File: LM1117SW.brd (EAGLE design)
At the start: 160 x 100 mm, 7 parts

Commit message: layout stuff
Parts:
- R1, R2: device rcl:R0402 -> rcl:R0603
- moved C1 33.5 mm to (2.32, 5.55), turned to 90 degrees
- moved C2 29.7 mm to (4.20, 5.55), turned to 90 degrees
- moved R2 28.9 mm to (1.89, 2.18), flipped to the bottom, turned to 90 degrees
- moved L1 27.9 mm to (3.55, 5.56), flipped to the bottom, turned to 90 degrees
- moved R1 27.7 mm to (4.50, 2.19), flipped to the bottom, turned to 270 degrees
- moved U$2 26.9 mm to (3.16, 2.04), turned to 270 degrees
- moved U$1 16.9 mm to (9.58, 3.98), turned to 270 degrees
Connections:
- net N$2 renamed VOUT
- net N$3 renamed SENS
- net N$4 renamed VIN
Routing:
- net VOUT: track 0.00 -> 12.9 mm, vias 0 -> 2
- net GND: track 0.00 -> 11.9 mm, vias 0 -> 1
- net SENS: track 0.00 -> 6.60 mm, vias 0 -> 1
- net N$1: track 0.00 -> 5.70 mm, vias 0 -> 1
- net VIN: track 0.00 -> 3.04 mm
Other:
- board size 160 x 100 mm -> 7.9 x 7.8 mm

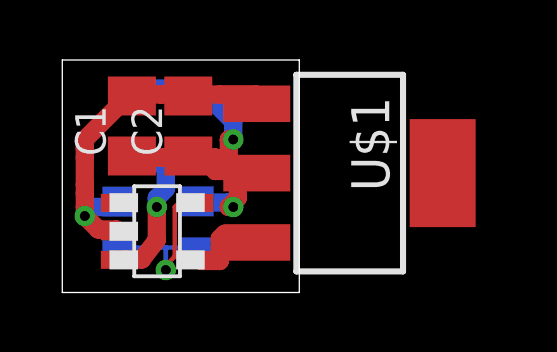
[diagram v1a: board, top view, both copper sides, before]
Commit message: finished LM1117 replacement
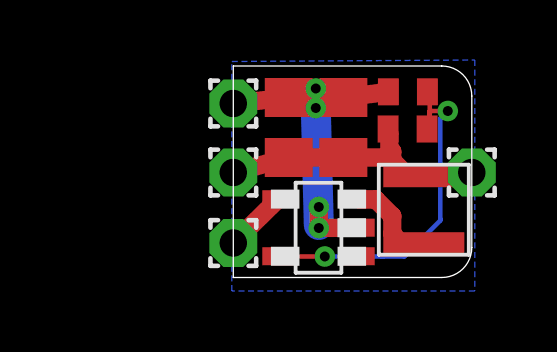
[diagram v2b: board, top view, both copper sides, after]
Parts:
- removed U$1: LM1117, Fabian:SOT223
- added PAD1, PAD2, PAD3, PAD4: (no value), wirepad:1,6/0,9
- R1, R2: device rcl:R0603 -> rcl:R0402
- moved R2 10.6 mm to (11.5, 6.69), flipped to the top, turned to 180 degrees
- moved L1 8.95 mm to (12.1, 2.76), flipped to the top
- moved R1 7.73 mm to (11.5, 5.45), flipped to the top, turned to 0 degrees
- moved C1 7.05 mm to (9.37, 5.50)
- moved U$2 5.38 mm to (8.54, 2.16), turned to 90 degrees
- moved C2 3.35 mm to (7.55, 5.50)
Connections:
- net GND: now also PAD3.1; no longer U$1.LEFT
- net VIN: now also PAD1.1; no longer U$1.RIGHT
- net VOUT: now also PAD2.1, PAD4.1; no longer U$1.MID
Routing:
- net SENS: track 6.60 -> 12.4 mm, vias 1 -> 2
- net VOUT: track 12.9 -> 8.01 mm, vias 2 -> 0
- net N$1: track 5.70 -> 3.15 mm, vias 1 -> 0
- net VIN: track 3.04 -> 2.09 mm
- net GND: track 11.9 -> 12.1 mm, vias 1 -> 4
- added copper zone on layer 16, net GND
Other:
- board size 7.9 x 7.8 mm -> 8 x 7 mm
- board text added: "huslik.net"

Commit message: updated order list
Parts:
- R1: value (none) -> 61k9
- R2: value (none) -> 20k
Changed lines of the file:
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@@
 <grid distance="0.05" unitdist="mm" unit="mm" style="lines" multiple="1" display="no" altdistance="0.05" altunitdist="mm" altunit="mm"/>
 <layers>
-<layer number="1" name="Top" color="4" fill="1" visible="no" active="yes"/>
+<layer number="1" name="Top" color="4" fill="1" visible="yes" active="yes"/>
 <layer number="2" name="Route2" color="1" fill="3" visible="no" active="no"/>
 <layer number="3" name="Route3" color="4" fill="3" visible="no" active="no"/>
@@
 <layer number="17" name="Pads" color="2" fill="1" visible="yes" active="yes"/>
 <layer number="18" name="Vias" color="2" fill="1" visible="yes" active="yes"/>
-<layer number="19" name="Unrouted" color="6" fill="1" visible="no" active="yes"/>
+<layer number="19" name="Unrouted" color="6" fill="1" visible="yes" active="yes"/>
 <layer number="20" name="Dimension" color="15" fill="1" visible="yes" active="yes"/>
-<layer number="21" name="tPlace" color="7" fill="1" visible="no" active="yes"/>
+<layer number="21" name="tPlace" color="7" fill="1" visible="yes" active="yes"/>
 <layer number="22" name="bPlace" color="7" fill="1" visible="yes" active="yes"/>
-<layer number="23" name="tOrigins" color="15" fill="1" visible="no" active="yes"/>
+<layer number="23" name="tOrigins" color="15" fill="1" visible="yes" active="yes"/>
 <layer number="24" name="bOrigins" color="15" fill="1" visible="yes" active="yes"/>
 <layer number="25" name="tNames" color="7" fill="1" visible="no" active="yes"/>
@@
 <layer number="48" name="Document" color="7" fill="1" visible="no" active="yes"/>
 <layer number="49" name="Reference" color="7" fill="1" visible="no" active="yes"/>
-<layer number="51" name="tDocu" color="7" fill="1" visible="no" active="yes"/>
+<layer number="51" name="tDocu" color="7" fill="1" visible="yes" active="yes"/>
 <layer number="52" name="bDocu" color="7" fill="1" visible="yes" active="yes"/>
 <layer number="90" name="Modules" color="5" fill="1" visible="no" active="no"/>
@@
 <elements>
 <element name="C1" library="rcl" package="C0805K" value="10uF" x="9.37" y="5.5" smashed="yes" rot="R90">
-<attribute name="OC_FARNELL" value="1759421" x="9.37" y="5.5" size="1.778" layer="27" rot="R90" display="off"/>
+<attribute name="OC_FARNELL" value="2320833" x="9.37" y="5.5" size="1.778" layer="27" rot="R90" display="off"/>
+<attribute name="MF" value="MULTICOMP" x="9.37" y="5.5" size="1.778" layer="27" rot="R90" display="off"/>
+<attribute name="MPN" value="MC0805X106K250CT" x="9.37" y="5.5" size="1.778" layer="27" rot="R90" display="off"/>
 </element>
 <element name="C2" library="rcl" package="C0805K" value="10uF" x="7.55" y="5.5" smashed="yes" rot="R90">
-<attribute name="OC_FARNELL" value="1759421" x="7.55" y="5.5" size="1.778" layer="27" rot="R90" display="off"/>
-</element>
-<element name="L1" library="Fabian" package="TYS3010100M-10" value="L_10UH_560MA" x="12.05" y="2.76" smashed="yes" rot="R90"/>
-<element name="R1" library="rcl" package="R0402" value="" x="11.51" y="5.45" smashed="yes">
+<attribute name="OC_FARNELL" value="2320833" x="7.55" y="5.5" size="1.778" layer="27" rot="R90" display="off"/>
+<attribute name="MF" value="MULTICOMP" x="7.55" y="5.5" size="1.778" layer="27" rot="R90" display="off"/>
+<attribute name="MPN" value="MC0805X106K250CT" x="7.55" y="5.5" size="1.778" layer="27" rot="R90" display="off"/>
+</element>
+<element name="L1" library="Fabian" package="TYS3010100M-10" value="L_10UH_560MA" x="12.05" y="2.76" smashed="yes" rot="R90">
+<attribute name="OC_FARNELL" value="2292503" x="12.05" y="2.76" size="1.778" layer="27" rot="R90" display="off"/>
+<attribute name="MF" value="LAIRD TECHNOLOGIES" x="12.05" y="2.76" size="1.778" layer="27" rot="R90" display="off"/>
+<attribute name="MPN" value="TYS3010100M-10" x="12.05" y="2.76" size="1.778" layer="27" rot="R90" display="off"/>
+</element>
+<element name="R1" library="rcl" package="R0402" value="61k9" x="11.51" y="5.45" smashed="yes">
 <attribute name="VALUE" x="10.875" y="3.545" size="1.27" layer="27"/>
-</element>
-<element name="R2" library="rcl" package="R0402" value="" x="11.52" y="6.69" smashed="yes" rot="R180">
+<attribute name="OC_FARNELL" value="1803730" x="11.51" y="5.45" size="1.778" layer="27" display="off"/>
+<attribute name="MF" value="MULTICOMP" x="11.51" y="5.45" size="1.778" layer="27" display="off"/>
+<attribute name="MPN" value="MC00625W0402161K9" x="11.51" y="5.45" size="1.778" layer="27" display="off"/>
+</element>
+<element name="R2" library="rcl" package="R0402" value="20k" x="11.52" y="6.69" smashed="yes" rot="R180">
 <attribute name="VALUE" x="12.155" y="8.595" size="1.27" layer="27" rot="R180"/>
-</element>
-<element name="U$2" library="Fabian" package="SOT23-5" value="TPS560200" x="8.54" y="2.16" smashed="yes" rot="R90"/>
+<attribute name="OC_FARNELL" value="1469693" x="11.52" y="6.69" size="1.778" layer="27" rot="R180" display="off"/>
+<attribute name="MF" value="VISHAY DRALORIC" x="11.52" y="6.69" size="1.778" layer="27" rot="R180" display="off"/>
+<attribute name="MPN" value="CRCW040220K0FKED" x="11.52" y="6.69" size="1.778" layer="27" rot="R180" display="off"/>
+</element>
+<element name="U$2" library="Fabian" package="SOT23-5" value="TPS560200" x="8.54" y="2.16" smashed="yes" rot="R90">
+<attribute name="OC_FARNELL" value="2373566" x="8.54" y="2.16" size="1.778" layer="27" rot="R90" display="off"/>
+<attribute name="MF" value="TEXAS INSTRUMENTS" x="8.54" y="2.16" size="1.778" layer="27" rot="R90" display="off"/>
+<attribute name="MPN" value="TPS560200DBVT" x="8.54" y="2.16" size="1.778" layer="27" rot="R90" display="off"/>
+</element>
 <element name="PAD1" library="wirepad" package="1,6/0,9" value="" x="5.7" y="1.65" smashed="yes">
 <attribute name="VALUE" x="5.7" y="2.25" size="0.0254" layer="27"/>
+<attribute name="OC_FARNELL" value="unknown" x="5.7" y="1.65" size="1.778" layer="27" display="off"/>
+<attribute name="MF" value="" x="5.7" y="1.65" size="1.778" layer="27" display="off"/>
+<attribute name="MPN" value="" x="5.7" y="1.65" size="1.778" layer="27" display="off"/>
 </element>
 <element name="PAD2" library="wirepad" package="1,6/0,9" value="" x="5.7" y="4" smashed="yes">
 <attribute name="VALUE" x="5.7" y="4.6" size="0.0254" layer="27"/>
+<attribute name="OC_FARNELL" value="unknown" x="5.7" y="4" size="1.778" layer="27" display="off"/>
+<attribute name="MF" value="" x="5.7" y="4" size="1.778" layer="27" display="off"/>
+<attribute name="MPN" value="" x="5.7" y="4" size="1.778" layer="27" display="off"/>
 </element>
 <element name="PAD3" library="wirepad" package="1,6/0,9" value="" x="5.7" y="6.3" smashed="yes">
 <attribute name="VALUE" x="5.7" y="6.9" size="0.0254" layer="27"/>
+<attribute name="OC_FARNELL" value="unknown" x="5.7" y="6.3" size="1.778" layer="27" display="off"/>
+<attribute name="MF" value="" x="5.7" y="6.3" size="1.778" layer="27" display="off"/>
+<attribute name="MPN" value="" x="5.7" y="6.3" size="1.778" layer="27" display="off"/>
 </element>
 <element name="PAD4" library="wirepad" package="1,6/0,9" value="" x="13.65" y="4" smashed="yes">
 <attribute name="VALUE" x="13.65" y="4.6" size="0.0254" layer="27"/>
+<attribute name="OC_FARNELL" value="unknown" x="13.65" y="4" size="1.778" layer="27" display="off"/>
+<attribute name="MF" value="" x="13.65" y="4" size="1.778" layer="27" display="off"/>
+<attribute name="MPN" value="" x="13.65" y="4" size="1.778" layer="27" display="off"/>
 </element>
 </elements>
